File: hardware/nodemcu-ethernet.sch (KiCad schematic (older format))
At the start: 8 parts

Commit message: Major documentation changes!
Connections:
- net at R2.1: now also D1.2 (K)
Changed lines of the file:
@@
 Sheet 1 1
 Title "NodeMCU 10-Base-T Wiring Diagram"
-Date "30 mar 2016"
+Date "1 apr 2016"
 Rev "-"
 Comp "(C) 2016 <>< Charles Lohr"
@@
 Text Notes 500  1650 0    60   ~ 0
 An antenna may be used instead\nof C3.  This is used to radiate\nhigher freuqencies to get a\ncleaner signal at 20 MHz.
+Wire Wire Line
+	2400 1500 2400 750
+Wire Wire Line
+	2400 750  2200 750
 $EndSCHEMATC

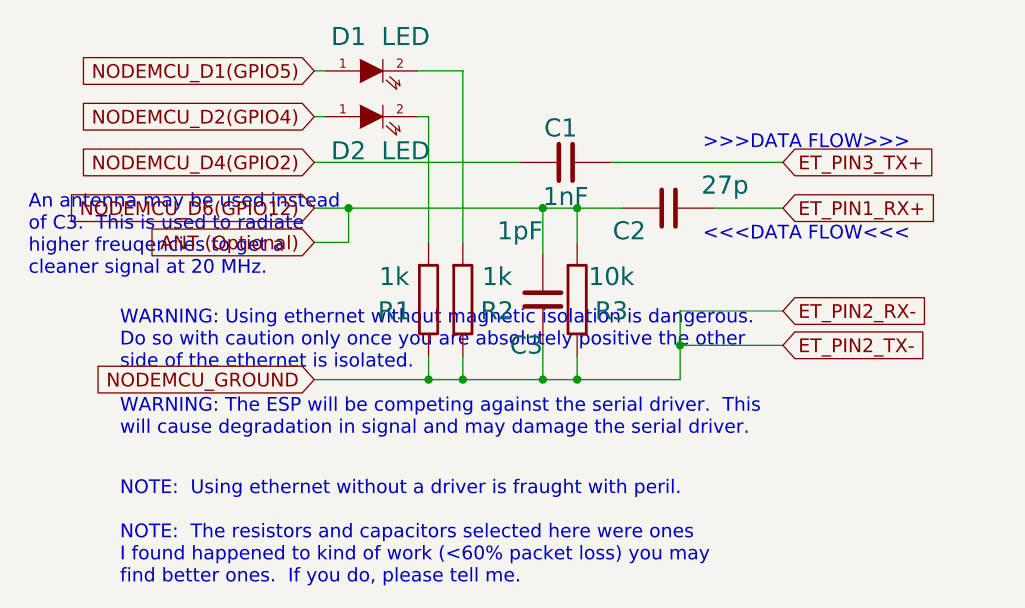
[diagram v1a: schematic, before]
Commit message: update schematic with better design
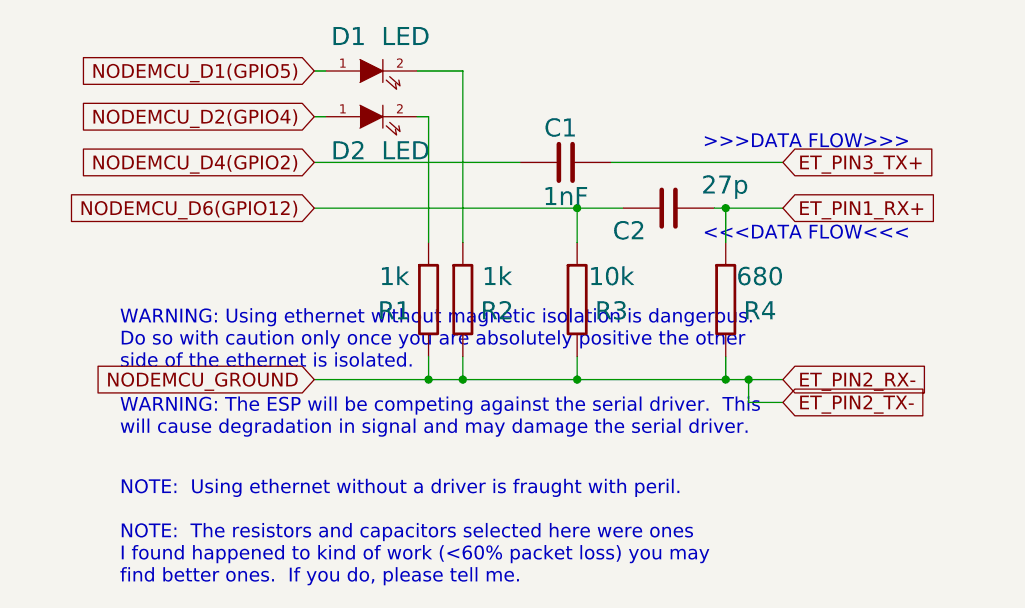
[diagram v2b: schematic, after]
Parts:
- removed C3: 1pF, ~, symbol C
- added R4: 680, ~, symbol R
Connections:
- net ET_PIN1_RX+: now also R4.1
- net ET_PIN2_RX-: now also R4.2
- net ANT (Optional) renamed NODEMCU_D6(GPIO12)
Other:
- note removed: "An antenna may be used instead\nof C3. This is used to radiate\nhigher freuqencies to get a\ncleaner signal at 20 MHz."
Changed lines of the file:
@@
 Sheet 1 1
 Title "NodeMCU 10-Base-T Wiring Diagram"
-Date "1 apr 2016"
+Date "2 apr 2016"
 Rev "-"
 Comp "(C) 2016 <>< Charles Lohr"
@@
 $EndComp
 Wire Wire Line
-	3350 2100 1750 2100
+	1750 2100 3800 2100
 Wire Wire Line
 	2400 2000 2400 2100
@@
 Text GLabel 3800 1150 2    60   Input ~ 0
 ET_PIN3_TX+
-Text GLabel 3800 1800 2    60   Input ~ 0
+Text GLabel 3800 2100 2    60   Input ~ 0
 ET_PIN2_RX-
-Text GLabel 3800 1950 2    60   Input ~ 0
+Text GLabel 3800 2200 2    60   Input ~ 0
 ET_PIN2_TX-
-Wire Wire Line
-	3800 1950 3350 1950
-Wire Wire Line
-	3350 1800 3350 2100
-Wire Wire Line
-	3350 1800 3800 1800
-Connection ~ 3350 1950
 Wire Wire Line
 	1800 950  1750 950
@@
 Wire Wire Line
 	2250 950  2250 1500
-$Comp
-L C C3
-U 1 1 56FB5B40
-P 2750 1750
-F 0 "C3" H 2750 1950 79  0000 L CNN
-F 1 "1pF" H 2750 1450 79  0000 L CNN
-F 2 "~" H 2788 1600 30  0000 C CNN
-F 3 "~" H 2750 1750 60  0000 C CNN
-	1    2750 1750
-	-1   0    0    1
-$EndComp
-Wire Wire Line
-	2750 1350 2750 1550
-Connection ~ 2750 1350
-Wire Wire Line
-	2750 1950 2750 2100
-Connection ~ 2750 2100
-Text GLabel 1750 1500 0    60   Input ~ 0
-ANT (Optional)
-Wire Wire Line
-	1750 1500 1900 1500
-Wire Wire Line
-	1900 1500 1900 1350
-Connection ~ 1900 1350
-Text Notes 500  1650 0    60   ~ 0
-An antenna may be used instead\nof C3.  This is used to radiate\nhigher freuqencies to get a\ncleaner signal at 20 MHz.
 Wire Wire Line
 	2400 1500 2400 750
 Wire Wire Line
 	2400 750  2200 750
+Wire Wire Line
+	3650 2100 3650 2200
+Wire Wire Line
+	3650 2200 3800 2200
+Connection ~ 3650 2100
+$Comp
+L R R4
+U 1 1 56FF541F
+P 3550 1750
+F 0 "R4" H 3700 1700 79  0000 C CNN
+F 1 "680" H 3700 1850 79  0000 C CNN
+F 2 "~" V 3480 1750 30  0000 C CNN
+F 3 "~" H 3550 1750 30  0000 C CNN
+	1    3550 1750
+	1    0    0    -1
+$EndComp
+Wire Wire Line
+	3550 1500 3550 1350
+Connection ~ 3550 1350
+Wire Wire Line
+	3550 2000 3550 2100
+Connection ~ 3550 2100
 $EndSCHEMATC
